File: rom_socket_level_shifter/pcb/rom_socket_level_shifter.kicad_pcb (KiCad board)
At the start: 2 copper layers, 17.8 x 35.6 mm, 45 parts

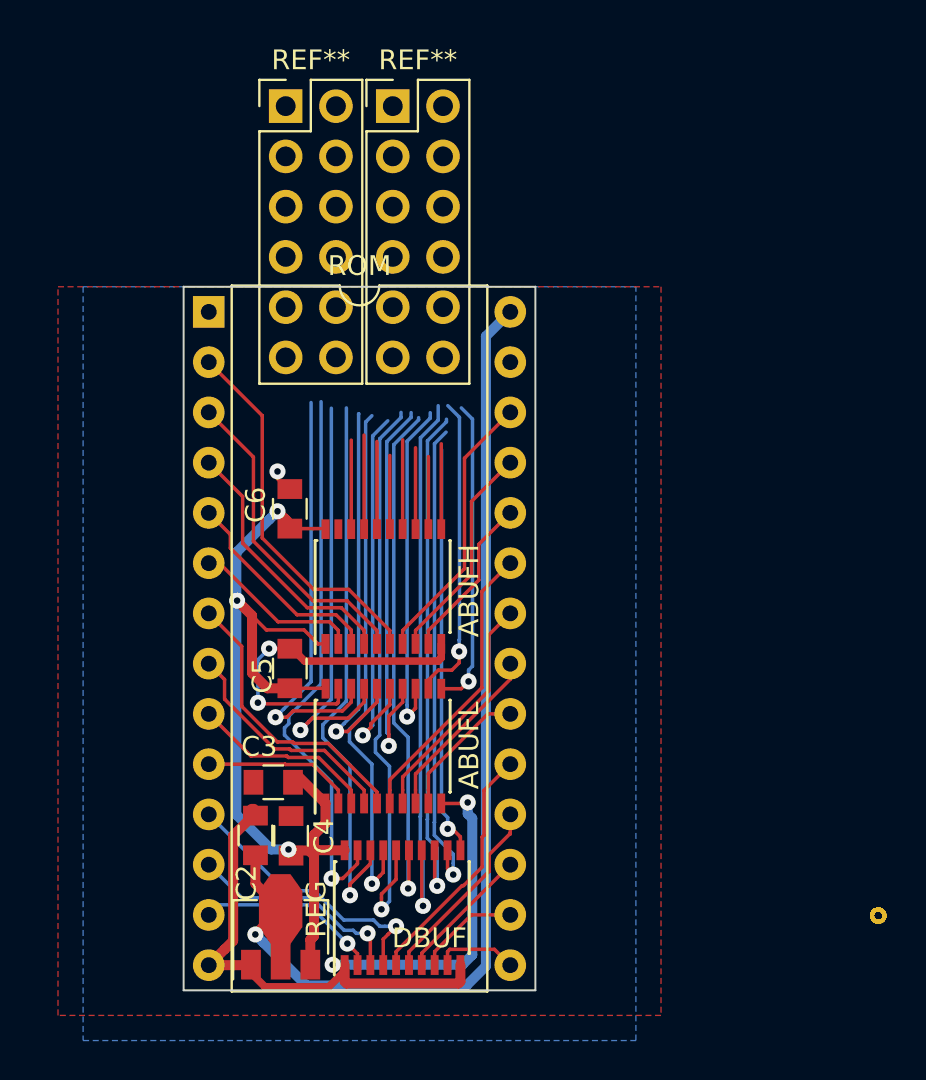
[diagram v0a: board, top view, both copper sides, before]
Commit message: rom_socket_level_shifter: DRC passes, board probably works, but looks extremely ugly
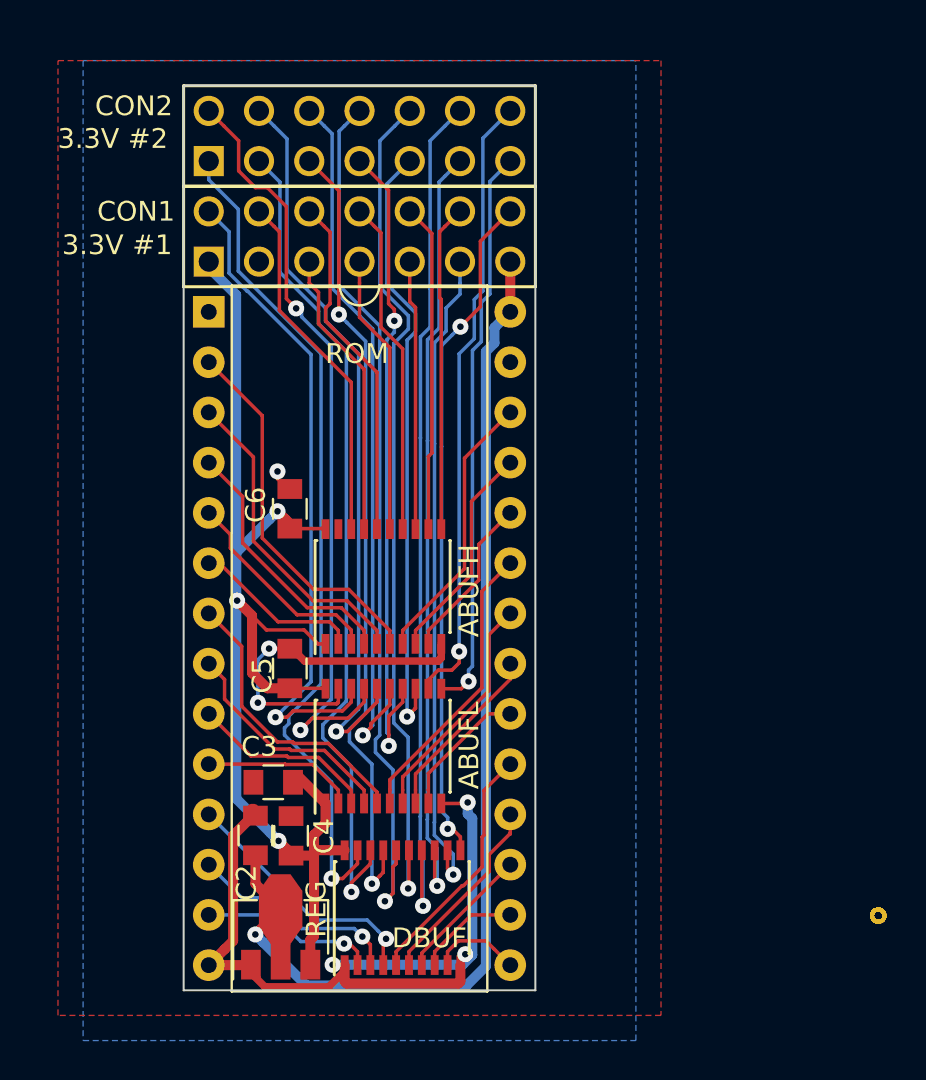
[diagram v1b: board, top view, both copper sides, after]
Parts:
- removed REF** (x2): Pin_Header_Straight_2x06_Pitch2.54mm, Pin_Headers:Pin_Header_Straight_2x06_Pitch2.54mm
- added CON1: 3.3V #1, myelin-kicad:header_2x07_100mil, F.Cu at (142.2, 44.5)
- added CON2: 3.3V #2, myelin-kicad:header_2x07_100mil, F.Cu at (142.2, 39.4)
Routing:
- net ext_A10: track 21.4 -> 39.8 mm, vias 1 -> 2
- net ext_nOE: track 19.9 -> 37.3 mm
- net ext_A11: track 19.3 -> 36.0 mm
- net ext_D6: track 26.6 -> 43.1 mm
- net ext_A1: track 15.6 -> 31.3 mm
- net ext_D7: track 28.5 -> 43.9 mm
- net ext_D5: track 29.4 -> 44.7 mm
- net 3V3: track 48.9 -> 63.7 mm
- net ext_dbuf_nCE: track 28.2 -> 42.7 mm
- net ext_D3: track 28.4 -> 42.4 mm
- net ext_D4: track 26.5 -> 40.4 mm, vias 1 -> 2
- net ext_A9: track 4.50 -> 18.0 mm
- net ext_A2: track 17.4 -> 30.9 mm
- net ext_D2: track 20.8 -> 34.3 mm, vias 1 -> 2
- net ext_D0: track 26.0 -> 39.4 mm
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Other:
- board size 17.8 x 35.6 mm -> 17.8 x 45.7 mm

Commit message: rom_socket_level_shifter v1 ready to fab
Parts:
- removed staple_single10, staple_single11, staple_single12, staple_single13, staple_single14, staple_single15, staple_single16, staple_single17, staple_single18, staple_single19, staple_single20, staple_single21, staple_single22, staple_single23, staple_single24, staple_single25, staple_single26, staple_single27, staple_single28, staple_single29, staple_single30, staple_single31, staple_single32, staple_single33, staple_single8, staple_single9: , myelin-kicad:via_single
- moved staple_single2 43.0 mm to (137.1, 49.4)
- moved staple_single5 27.4 mm to (141.4, 74.6)
- moved staple_single4 27.0 mm to (141.5, 80.5)
- moved staple_single7 26.4 mm to (147.6, 62.5)
- moved staple_single1 23.3 mm to (147.6, 68.3)
- moved staple_single6 22.9 mm to (146.0, 74.3)
- moved staple_single3 21.2 mm to (147.3, 80.5)
- moved ABUFH 7.24 mm to (143.4, 54.9)
- moved C6 5.97 mm to (138.6, 52.3)
- moved ABUFL 5.04 mm to (143.4, 65.2)
- moved C5 3.70 mm to (138.6, 62.6), turned to 90 degrees
- moved DBUF 2.44 mm to (144.4, 75.9)
- moved C3 1.12 mm to (137.9, 70.9)
- moved C4 1.01 mm to (138.8, 73.7)
- moved REG 1.00 mm to (138.3, 78.8)
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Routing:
- net GND: track 61.0 -> 21.6 mm, vias 6 -> 4
- net ext_A10: track 39.8 -> 28.3 mm
- net ext_A3: track 33.7 -> 22.8 mm
- net ext_nCS: track 33.3 -> 22.9 mm
- net ext_nOE: track 37.3 -> 26.9 mm
- net ext_A11: track 36.0 -> 25.9 mm
- net ext_A2: track 30.9 -> 22.7 mm
- net ext_D7: track 43.9 -> 36.2 mm
- net ext_D3: track 42.4 -> 34.9 mm
- net ext_D5: track 44.7 -> 37.3 mm
- net ext_A5: track 16.6 -> 9.28 mm
- net ext_A4: track 16.5 -> 9.28 mm
- net ext_A8: track 14.7 -> 7.42 mm
- net ext_A6: track 13.6 -> 6.40 mm
- net ext_A7: track 17.0 -> 9.72 mm
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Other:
- board text added: "BBC Model B ROM socket level shifter Phillip Pearson Copyright 2017 Google LLC http://myelin.nz/acorn/romshift"

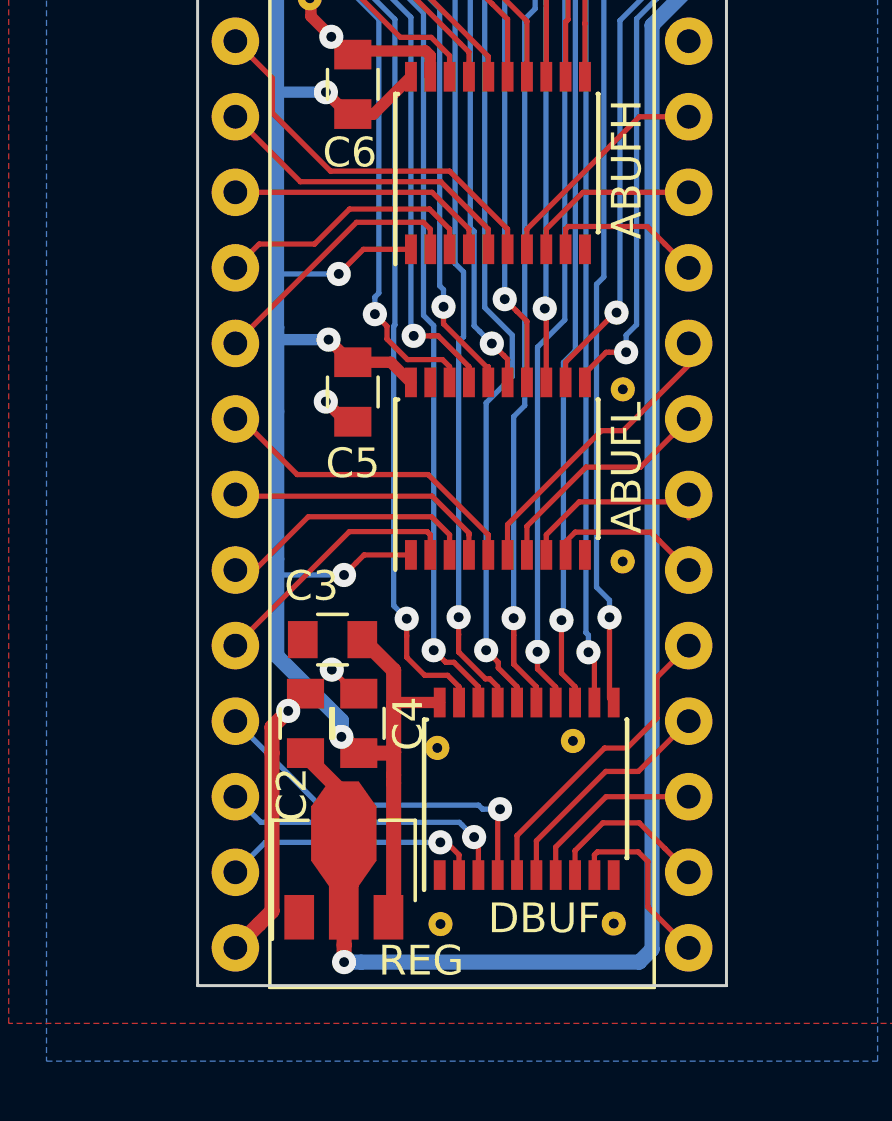
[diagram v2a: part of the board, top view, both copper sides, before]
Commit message: rom_socket_level_shifter v2: Added pullup resistor to /CE on DBUF
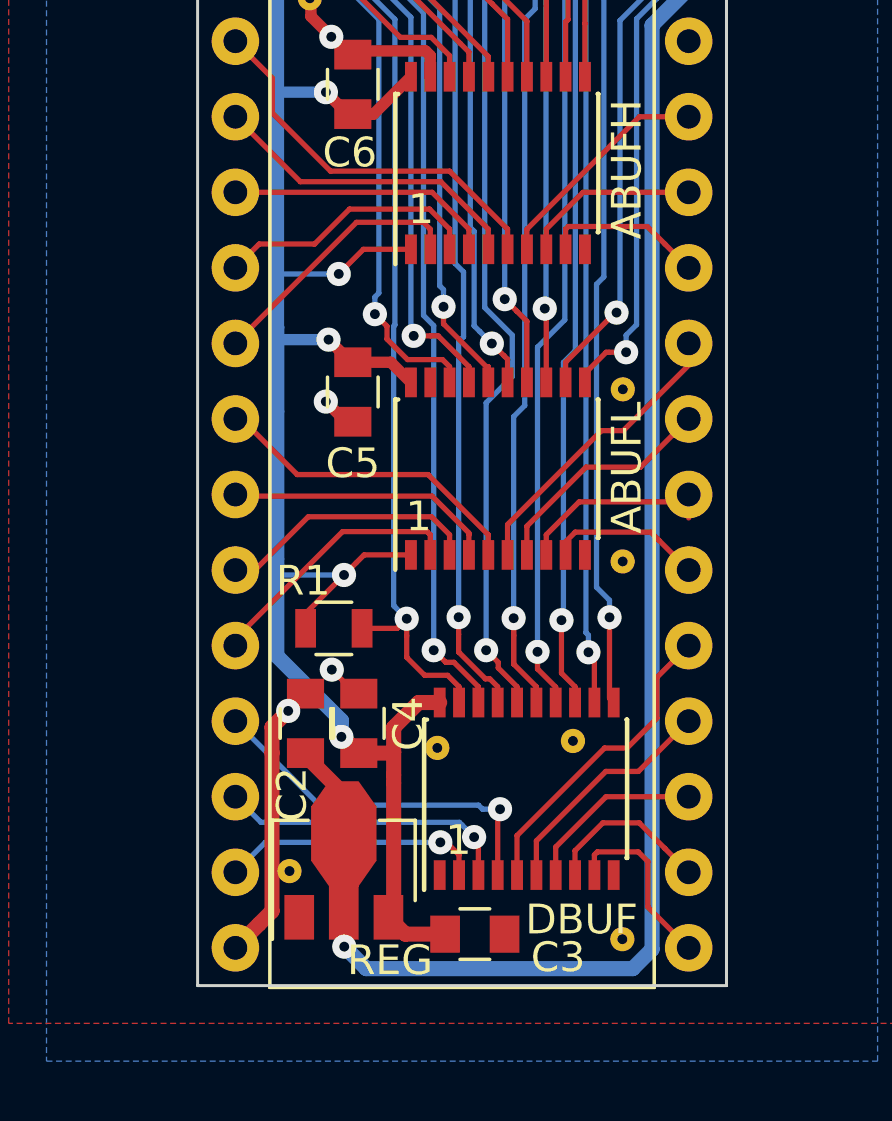
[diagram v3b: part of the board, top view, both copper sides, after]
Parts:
- added R1: 19k, Resistors_SMD:R_0805, F.Cu at (137.9, 70.5)
- moved C3 11.0 mm to (142.7, 80.8), turned to 0 degrees
- moved staple_single4 5.38 mm to (136.4, 78.7)
- moved staple_single3 0.60 mm to (147.6, 81.0)
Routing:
- net ext_dbuf_nCE: track 36.0 -> 37.6 mm
- net 3V3: track 63.4 -> 64.7 mm
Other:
- board text added: "1"
- board text added: "BBC Model B ROM socket level shifter r2 Phillip Pearson Copyright 2017 Google LLC http://myelin.nz/acorn/romshift"
- board text removed: "BBC Model B ROM socket level shifter Phillip Pearson Copyright 2017 Google LLC http://myelin.nz/acorn/romshift"
